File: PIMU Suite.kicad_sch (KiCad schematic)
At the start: 15 parts, among them U2 MICROSD_SPI_OR_SDIO_CARD

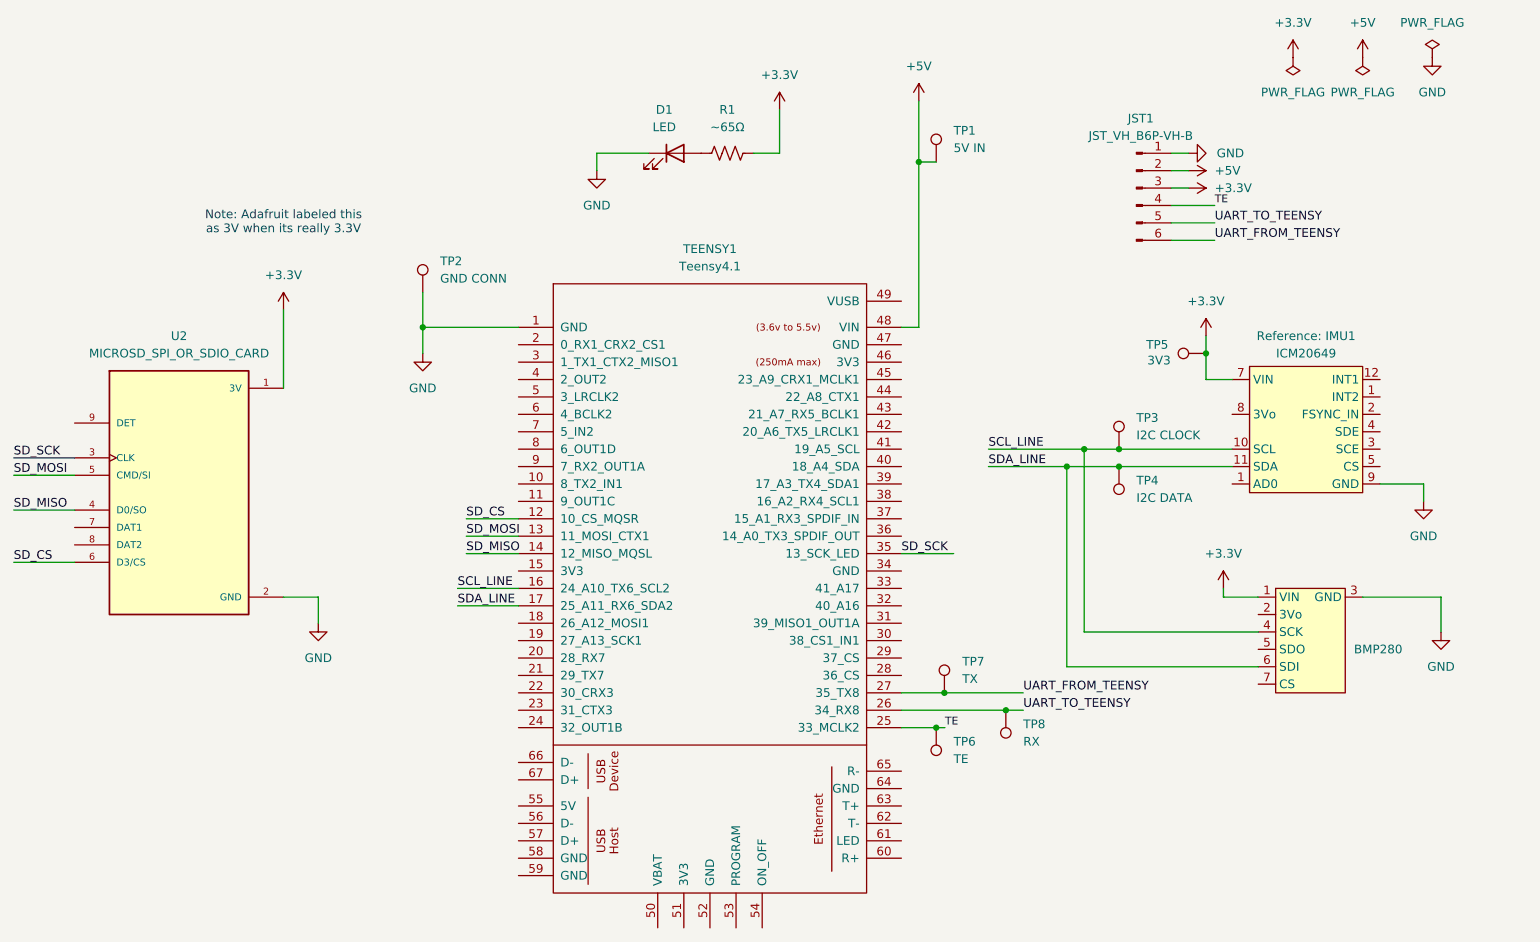
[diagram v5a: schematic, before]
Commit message: USB headers + silkscreen
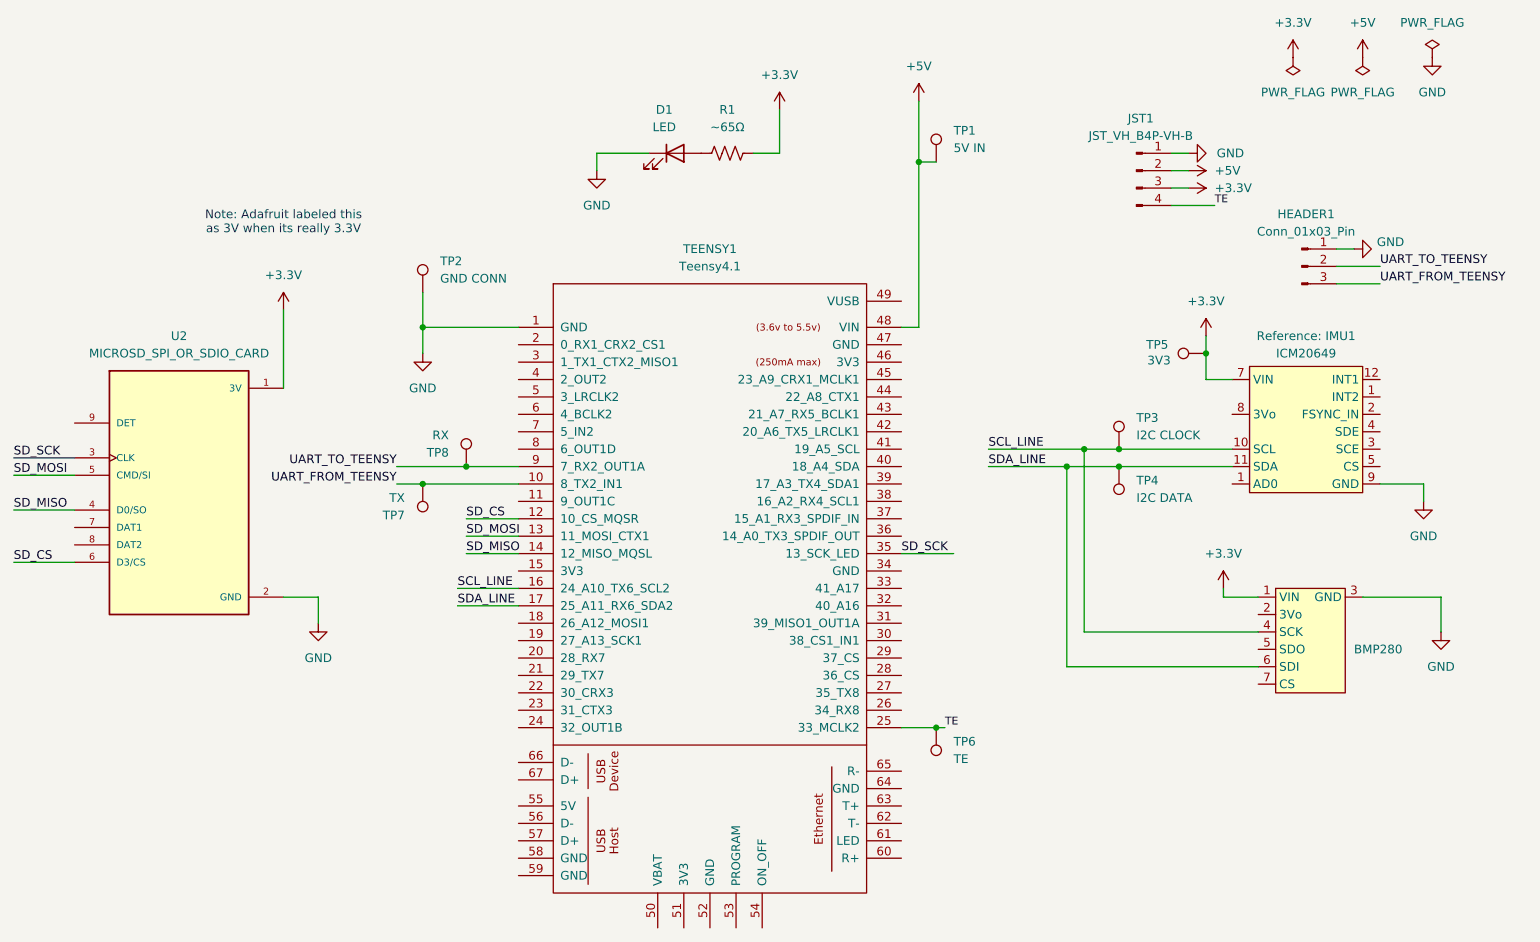
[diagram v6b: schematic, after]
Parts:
- added HEADER1: Conn_01x03_Pin, Connector_PinHeader_2.54mm:PinHeader_1x03_P2.54mm_Vertical, symbol Connector:Conn_01x03_Pin
- JST1: value JST_VH_B6P-VH-B -> JST_VH_B4P-VH-B; footprint Connector_JST:JST_VH_B6P-VH-B_1x06_P3.96mm_Vertical -> Connector_JST:JST_VH_B4P-VH-B_1x04_P3.96mm_Vertical; symbol Connector:Conn_01x06_Pin -> Connector:Conn_01x04_Pin
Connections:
- net GND: now also HEADER1.1 (Pin_1)
- net UART_FROM_TEENSY: now also TEENSY1.10 (8_TX2_IN1), HEADER1.3 (Pin_3); no longer JST1.6 (Pin_6), TEENSY1.27 (35_TX8)
- net UART_TO_TEENSY: now also TEENSY1.9 (7_RX2_OUT1A), HEADER1.2 (Pin_2); no longer JST1.5 (Pin_5), TEENSY1.26 (34_RX8)
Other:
- moved on the sheet: TP7, TP8
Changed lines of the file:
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@@
+	)
+	(junction
+		(at 109.22 80.01)
+		(diameter 0)
+		(color 0 0 0 0)
 	)
 	(junction
@@
 	)
 	(junction
-		(at 178.9926 113.03)
-		(diameter 0)
-		(color 0 0 0 0)
-	)
-	(junction
-		(at 187.96 115.57)
-		(diameter 0)
-		(color 0 0 0 0)
-	)
-	(junction
 		(at 199.39 77.47)
 		(diameter 0)
@@
 	)
 	(junction
+		(at 102.87 82.55)
+		(diameter 0)
+		(color 0 0 0 0)
+	)
+	(junction
 		(at 177.8 118.11)
 		(diameter 0)
@@
 	(wire
 		(pts
-			(xy 212.09 46.99) (xy 218.44 46.99)
-		)
-		(stroke
-			(width 0)
-			(type default)
-		)
-	)
-	(wire
-		(pts
-			(xy 212.09 44.45) (xy 218.44 44.45)
+			(xy 236.22 53.34) (xy 242.57 53.34)
+		)
+		(stroke
+			(width 0)
+			(type default)
+		)
+	)
+	(wire
+		(pts
+			(xy 236.22 50.8) (xy 242.57 50.8)
 		)
 		(stroke
@@
 	(wire
 		(pts
-			(xy 187.96 115.57) (xy 190.5 115.57)
+			(xy 99.06 80.01) (xy 109.22 80.01)
 		)
 		(stroke
@@
 	(wire
 		(pts
+			(xy 238.76 48.26) (xy 236.22 48.26)
+		)
+		(stroke
+			(width 0)
+			(type default)
+		)
+	)
+	(wire
+		(pts
 			(xy 204.47 80.01) (xy 220.98 80.01)
 		)
@@
 	(wire
 		(pts
+			(xy 102.87 82.55) (xy 99.06 82.55)
+		)
+		(stroke
+			(width 0)
+			(type default)
+		)
+	)
+	(wire
+		(pts
 			(xy 135.89 34.29) (xy 128.27 34.29)
 		)
@@
 	(wire
 		(pts
-			(xy 172.72 115.57) (xy 187.96 115.57)
-		)
-		(stroke
-			(width 0)
-			(type default)
-		)
-	)
-	(wire
-		(pts
-			(xy 172.72 113.03) (xy 178.9926 113.03)
+			(xy 116.84 80.01) (xy 109.22 80.01)
 		)
 		(stroke
@@
 	(wire
 		(pts
-			(xy 178.9926 113.03) (xy 190.5 113.03)
+			(xy 102.87 82.55) (xy 116.84 82.55)
 		)
 		(stroke
@@
 	)
 	(label "UART_TO_TEENSY"
-		(at 190.5 115.57 0)
+		(at 99.06 80.01 180)
 		(effects
 			(font
 				(size 1.27 1.27)
 			)
-			(justify left bottom)
+			(justify right bottom)
 		)
 	)
@@
 	)
 	(label "UART_FROM_TEENSY"
-		(at 218.44 46.99 0)
+		(at 242.57 53.34 0)
 		(effects
 			(font
@@
 	)
 	(label "UART_TO_TEENSY"
-		(at 218.44 44.45 0)
+		(at 242.57 50.8 0)
 		(effects
 			(font
@@
 	)
 	(label "UART_FROM_TEENSY"
-		(at 190.5 113.03 0)
+		(at 99.06 82.55 180)
 		(effects
 			(font
 				(size 1.27 1.27)
 			)
-			(justify left bottom)
+			(justify right bottom)
 		)
 	)
@@
 	(symbol
 		(lib_id "Connector:TestPoint")
-		(at 178.9926 113.03 0)
+		(at 102.87 82.55 180)
 		(unit 1)
 		(exclude_from_sim no)
@@
 		(fields_autoplaced yes)
 		(property "Reference" "TP7"
-			(at 181.61 108.4579 0)
+			(at 100.2526 87.1221 0)
 			(effects
 				(font
@@
 		)
 		(property "Value" "TX"
-			(at 181.61 110.9979 0)
+			(at 100.2526 84.5821 0)
 			(effects
 				(font
@@
 		)
 		(property "Footprint" "TestPoint:TestPoint_Pad_D1.5mm"
-			(at 184.0726 113.03 0)
+			(at 97.79 82.55 0)
 			(effects
 				(font
@@
 		)
 		(property "Datasheet" "~"
-			(at 184.0726 113.03 0)
+			(at 97.79 82.55 0)
 			(effects
 				(font
@@
 		)
 		(property "Description" "GND"
-			(at 178.9926 113.03 0)
+			(at 102.87 82.55 0)
 			(effects
 				(font
@@
 	)
 	(symbol
-		(lib_id "Connector:Conn_01x06_Pin")
-		(at 207.01 39.37 0)
+		(lib_id "Connector:Conn_01x04_Pin")
+		(at 207.01 36.83 0)
 		(unit 1)
 		(exclude_from_sim no)
@@
 			)
 		)
-		(property "Value" "JST_VH_B6P-VH-B"
+		(property "Value" "JST_VH_B4P-VH-B"
 			(at 207.645 31.75 0)
 			(effects
@@
 			)
 		)
-		(property "Footprint" "Connector_JST:JST_VH_B6P-VH-B_1x06_P3.96mm_Vertical"
-			(at 207.01 39.37 0)
+		(property "Footprint" "Connector_JST:JST_VH_B4P-VH-B_1x04_P3.96mm_Vertical"
+			(at 207.01 36.83 0)
 			(effects
 				(font
@@
 		)
 		(property "Datasheet" "~"
-			(at 207.01 39.37 0)
-			(effects
-				(font
-					(size 1.27 1.27)
-				)
-				(hide yes)
-			)
-		)
-		(property "Description" "Generic connector, single row, 01x06, script generated"
-			(at 207.01 39.37 0)
+			(at 207.01 36.83 0)
+			(effects
+				(font
+					(size 1.27 1.27)
+				)
+				(hide yes)
+			)
+		)
+		(property "Description" "Generic connector, single row, 01x04, script generated"
+			(at 207.01 36.83 0)
 			(effects
 				(font
@@
 		)
 		(property "PARTREV" "27-1-20"
-			(at 207.01 39.37 0)
+			(at 207.01 36.83 0)
 			(effects
 				(font
@@
 		)
 		(property "STANDARD" "Manufacturer Recommendations"
-			(at 207.01 39.37 0)
+			(at 207.01 36.83 0)
 			(effects
 				(font
@@
 		)
 		(property "MAXIMUM_PACKAGE_HEIGHT" "6.1mm"
-			(at 207.01 39.37 0)
+			(at 207.01 36.83 0)
 			(effects
 				(font
@@
 		)
 		(property "MANUFACTURER" "JST"
-			(at 207.01 39.37 0)
+			(at 207.01 36.83 0)
 			(effects
 				(font
@@
 		)
 		(pin "4"
-		)
-		(pin "5"
-		)
-		(pin "6"
 		)
 		(instances
@@
 	(symbol
 		(lib_id "Connector:TestPoint")
-		(at 187.96 115.57 180)
+		(at 109.22 80.01 0)
 		(unit 1)
 		(exclude_from_sim no)
@@
 		(fields_autoplaced yes)
 		(property "Reference" "TP8"
-			(at 190.5 117.6019 0)
+			(at 106.68 77.9781 0)
 			(effects
 				(font
@@
 		)
 		(property "Value" "RX"
-			(at 190.5 120.1419 0)
+			(at 106.68 75.4381 0)
 			(effects
 				(font
@@
 		)
 		(property "Footprint" "TestPoint:TestPoint_Pad_D1.5mm"
-			(at 182.88 115.57 0)
+			(at 114.3 80.01 0)
 			(effects
 				(font
@@
 		)
 		(property "Datasheet" "~"
-			(at 182.88 115.57 0)
+			(at 114.3 80.01 0)
 			(effects
 				(font
@@
 		)
 		(property "Description" "GND"
-			(at 187.96 115.57 0)
+			(at 109.22 80.01 0)
 			(effects
 				(font
@@
 	)
 	(symbol
+		(lib_id "Connector:Conn_01x03_Pin")
+		(at 231.14 50.8 0)
+		(unit 1)
+		(exclude_from_sim no)
+		(in_bom yes)
+		(on_board yes)
+		(dnp no)
+		(fields_autoplaced yes)
+		(property "Reference" "HEADER1"
+			(at 231.775 43.18 0)
+			(effects
+				(font
+					(size 1.27 1.27)
+				)
+			)
+		)
+		(property "Value" "Conn_01x03_Pin"
+			(at 231.775 45.72 0)
+			(effects
+				(font
+					(size 1.27 1.27)
+				)
+			)
+		)
+		(property "Footprint" "Connector_PinHeader_2.54mm:PinHeader_1x03_P2.54mm_Vertical"
+			(at 231.14 50.8 0)
+			(effects
+				(font
+					(size 1.27 1.27)
+				)
+				(hide yes)
+			)
+		)
+		(property "Datasheet" "~"
+			(at 231.14 50.8 0)
+			(effects
+				(font
+					(size 1.27 1.27)
+				)
+				(hide yes)
+			)
+		)
+		(property "Description" "Generic connector, single row, 01x03, script generated"
+			(at 231.14 50.8 0)
+			(effects
+				(font
+					(size 1.27 1.27)
+				)
+				(hide yes)
+			)
+		)
+		(pin "2"
+		)
+		(pin "3"
+		)
+		(pin "1"
+		)
+		(instances
+			(project ""
+				(path "/f92a9e59-93af-435a-9a9e-44bda57be41a"
+					(reference "HEADER1")
+					(unit 1)
+				)
+			)
+		)
+	)
+	(symbol
 		(lib_id "Device:LED")
 		(at 139.7 34.29 0)
@@
 					(unit 1)
 				)
+			)
+		)
+	)
+	(symbol
+		(lib_id "power:GND")
+		(at 238.76 48.26 90)
+		(unit 1)
+		(exclude_from_sim no)
+		(in_bom yes)
+		(on_board yes)
+		(dnp no)
+		(property "Reference" "#PWR017"
+			(at 245.11 48.26 0)
+			(effects
+				(font
+					(size 1.27 1.27)
+				)
+				(hide yes)
+			)
+		)
+		(property "Value" "GND"
+			(at 244.094 47.244 90)
+			(effects
+				(font
+					(size 1.27 1.27)
+				)
+			)
+		)
+		(property "Footprint" ""
+			(at 238.76 48.26 0)
+			(effects
+				(font
+					(size 1.27 1.27)
+				)
+				(hide yes)
+			)
+		)
+		(property "Datasheet" ""
+			(at 238.76 48.26 0)
+			(effects
+				(font
+					(size 1.27 1.27)
+				)
+				(hide yes)
+			)
+		)
+		(property "Description" "Power symbol creates a global label with name \"GND\" , ground"
+			(at 238.76 48.26 0)
+			(effects
+				(font
+					(size 1.27 1.27)
+				)
+				(hide yes)
+			)
+		)
+		(pin "1"
+		)
+		(instances
+			(project "PIMU Suite"
+				(path "/f92a9e59-93af-435a-9a9e-44bda57be41a"
+					(reference "#PWR017")
+					(unit 1)
+				)
